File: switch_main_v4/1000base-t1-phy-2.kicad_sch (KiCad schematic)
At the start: 39 parts, among them Q1501 DMN21D2UFB-7B, Q1502 DMP21D0UFB-7B, U1501 TPS62290TDRVRQ1, U1502 88Q2112-A2-NYD2A000-P123

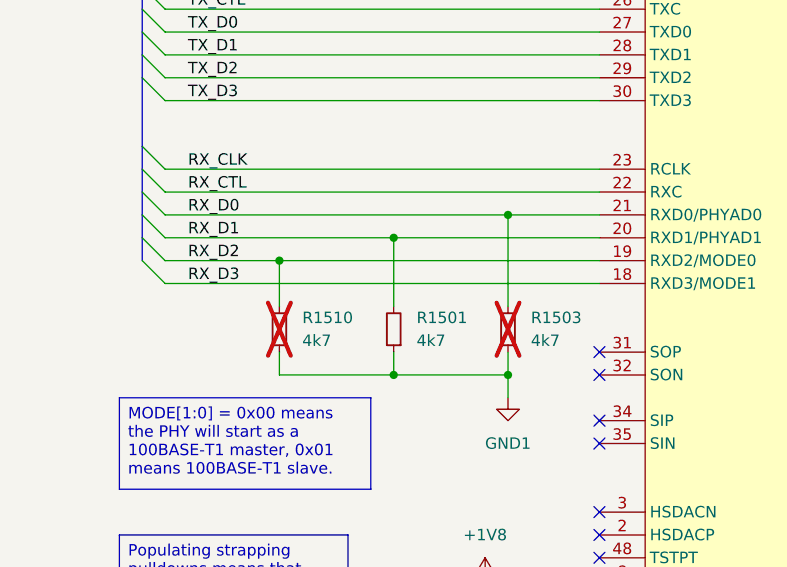
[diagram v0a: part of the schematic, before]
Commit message: Fixed mistake where RMII TX and RX signals were swapped
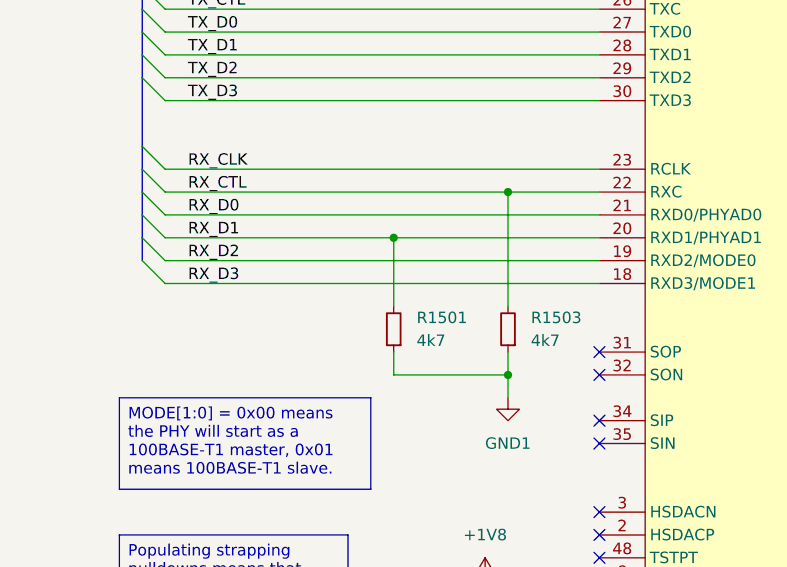
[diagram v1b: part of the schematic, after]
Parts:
- removed R1510: 4k7, Resistor_SMD:R_0402_1005Metric, symbol Device:R_Small
- R1503: now fitted; now in the parts list
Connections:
- net RX_CTL: now also R1503.2
- net RX_D0: no longer R1503.2
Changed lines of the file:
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@@
 	)
 	(junction
-		(at 71.12 106.68)
-		(diameter 0)
-		(color 0 0 0 0)
-	)
-	(junction
 		(at 226.06 55.88)
 		(diameter 0)
@@
 	)
 	(junction
-		(at 45.72 111.76)
-		(diameter 0)
-		(color 0 0 0 0)
-	)
-	(junction
 		(at 195.58 91.44)
 		(diameter 0)
@@
 	)
 	(junction
-		(at 58.42 124.46)
+		(at 71.12 104.14)
 		(diameter 0)
 		(color 0 0 0 0)
@@
 	(wire
 		(pts
-			(xy 45.72 111.76) (xy 81.28 111.76)
-		)
-		(stroke
-			(width 0)
-			(type default)
-		)
-	)
-	(wire
-		(pts
-			(xy 45.72 111.76) (xy 45.72 116.84)
-		)
-		(stroke
-			(width 0)
-			(type default)
-		)
-	)
-	(wire
-		(pts
 			(xy 121.92 139.7) (xy 154.94 139.7)
 		)
@@
 	(wire
 		(pts
-			(xy 45.72 121.92) (xy 45.72 124.46)
+			(xy 71.12 104.14) (xy 81.28 104.14)
 		)
 		(stroke
@@
 	(wire
 		(pts
-			(xy 33.02 111.76) (xy 45.72 111.76)
+			(xy 33.02 111.76) (xy 81.28 111.76)
 		)
 		(stroke
@@
 	(wire
 		(pts
-			(xy 71.12 106.68) (xy 81.28 106.68)
+			(xy 134.62 43.18) (xy 147.32 43.18)
 		)
 		(stroke
@@
 	(wire
 		(pts
-			(xy 134.62 43.18) (xy 147.32 43.18)
+			(xy 121.92 165.1) (xy 124.46 165.1)
 		)
 		(stroke
@@
 	(wire
 		(pts
-			(xy 121.92 165.1) (xy 124.46 165.1)
+			(xy 71.12 104.14) (xy 71.12 116.84)
 		)
 		(stroke
@@
 	(wire
 		(pts
-			(xy 71.12 106.68) (xy 71.12 116.84)
-		)
-		(stroke
-			(width 0)
-			(type default)
-		)
-	)
-	(wire
-		(pts
 			(xy 213.36 66.04) (xy 213.36 63.5)
 		)
@@
 	(wire
 		(pts
-			(xy 33.02 106.68) (xy 71.12 106.68)
+			(xy 33.02 106.68) (xy 81.28 106.68)
 		)
 		(stroke
@@
 		)
 	)
-	(wire
-		(pts
-			(xy 45.72 124.46) (xy 58.42 124.46)
-		)
-		(stroke
-			(width 0)
-			(type default)
-		)
-	)
 	(bus
 		(pts
@@
 	(wire
 		(pts
-			(xy 33.02 104.14) (xy 81.28 104.14)
+			(xy 33.02 104.14) (xy 71.12 104.14)
 		)
 		(stroke
@@
 	)
 	(symbol
-		(lib_id "Device:R_Small")
-		(at 45.72 119.38 180)
-		(unit 1)
-		(exclude_from_sim no)
-		(in_bom no)
-		(on_board no)
-		(dnp yes)
-		(fields_autoplaced yes)
-		(property "Reference" "R1510"
-			(at 48.26 118.1099 0)
-			(effects
-				(font
-					(size 1.27 1.27)
-				)
-				(justify right)
-			)
-		)
-		(property "Value" "4k7"
-			(at 48.26 120.6499 0)
-			(effects
-				(font
-					(size 1.27 1.27)
-				)
-				(justify right)
-			)
-		)
-		(property "Footprint" "Resistor_SMD:R_0402_1005Metric"
-			(at 45.72 119.38 0)
-			(effects
-				(font
-					(size 1.27 1.27)
-				)
-				(hide yes)
-			)
-		)
-		(property "Datasheet" "~"
-			(at 45.72 119.38 0)
-			(effects
-				(font
-					(size 1.27 1.27)
-				)
-				(hide yes)
-			)
-		)
-		(property "Description" "Resistor, small symbol"
-			(at 45.72 119.38 0)
-			(effects
-				(font
-					(size 1.27 1.27)
-				)
-				(hide yes)
-			)
-		)
-		(pin "2"
-		)
-		(pin "1"
-		)
-		(instances
-			(project "switch_main_v4"
-				(path "/a5e57332-4284-4d3c-ab3c-13bc0ddb29b6/71322af8-b569-498c-a6bf-684e9909732c/5b05d4e8-554f-4b77-b2ef-3843e3d18685"
-					(reference "R1510")
-					(unit 1)
-				)
-			)
-		)
-	)
-	(symbol
 		(lib_id "Device:C_Small")
 		(at 137.16 149.86 90)
@@
 		(unit 1)
 		(exclude_from_sim no)
-		(in_bom no)
-		(on_board no)
-		(dnp yes)
+		(in_bom yes)
+		(on_board yes)
+		(dnp no)
 		(fields_autoplaced yes)
 		(property "Reference" "R1503"
